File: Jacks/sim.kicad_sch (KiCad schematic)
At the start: 14 parts

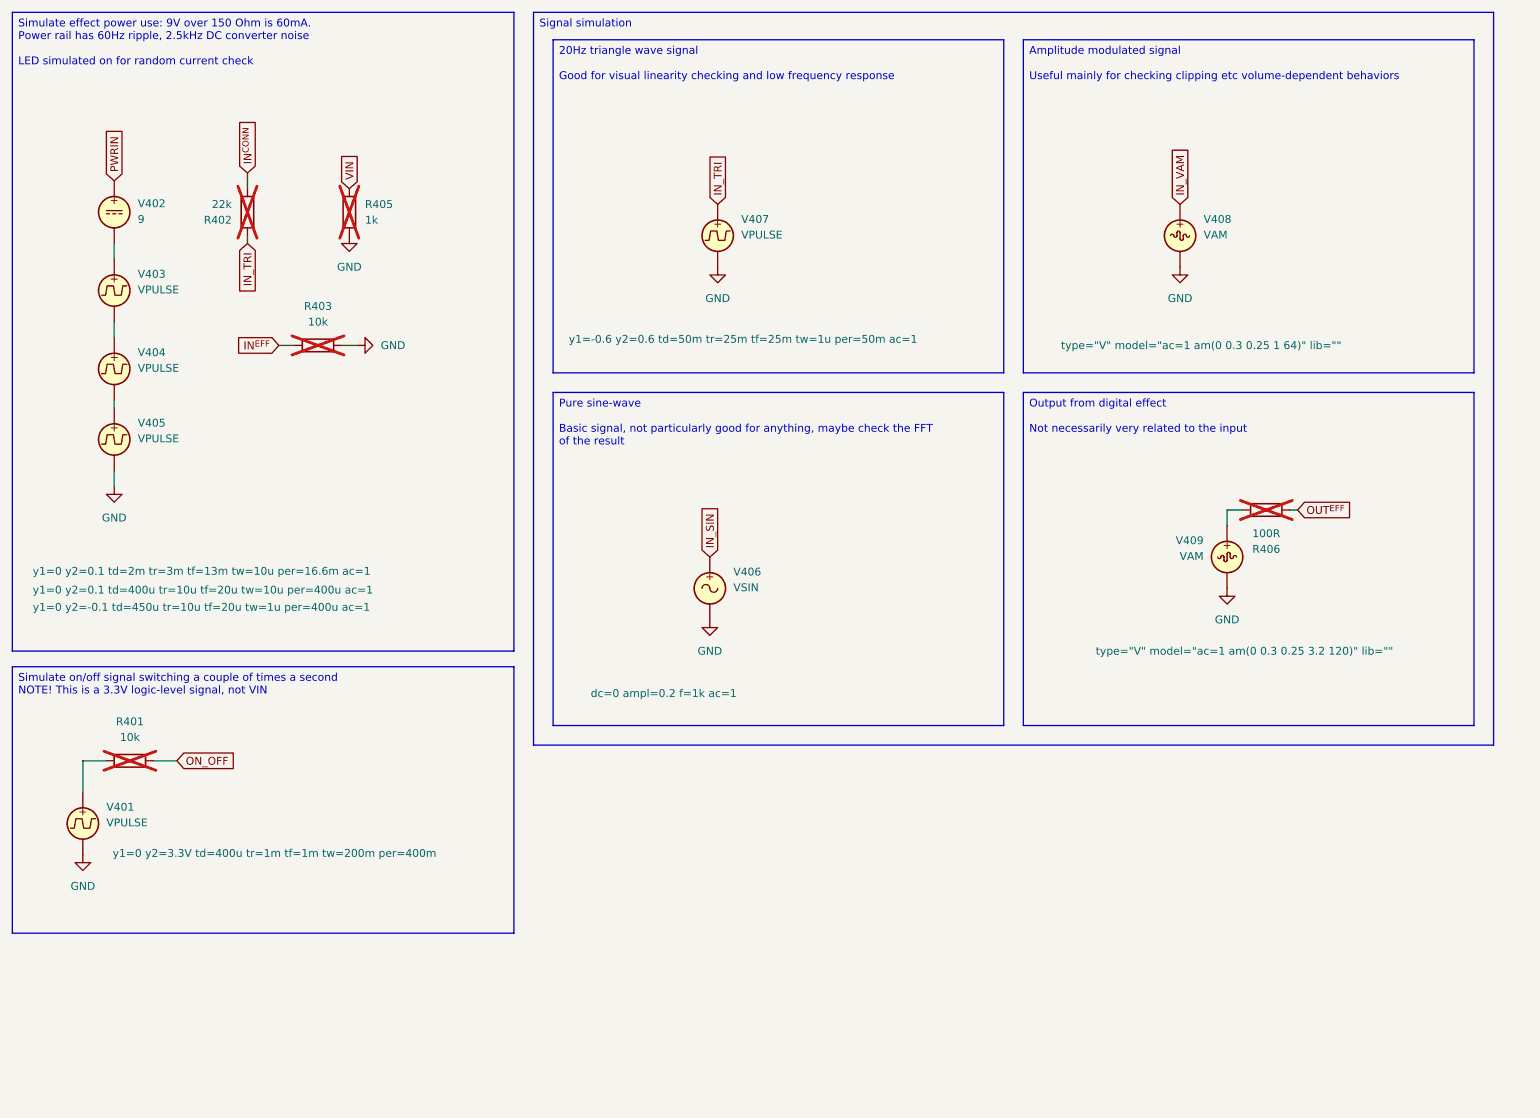
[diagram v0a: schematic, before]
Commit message: Trial attempt at different analog rail filtering
This does the +VA net a bit differently: by using a common collector
series follower transistor I can use much bigger resistors in the
lowpass filter because the current through the resistor is just the tiny
base current.

In fact, let's just make it the main filtering stage, and share the
resulting +VA rail for both the input stage and the output bias.  They
both need on the order of one mA of current, so assuming a DC current
gain (whether you call it h_{FE} or Beta) of roughly one hundred, we can
easily use a couple of 2k2 resistors and make it a 2nd order filter.

(The original used a single 220 Ohm resistor, so this increases that by
a factor of twenty, but then the h_{FE} will more than make up for it)

Of course, the small viltage drop over the resistors will now be almost
entirely dwarfed by the V_{BE} voltage drop of the transistor.  But if
it gives us a nice stable analog voltage rail, it should be worth the
small voltage drop.

I use a MOSFET for reverse polarity protection because I don't like the
voltage drop of a simple diode, but that's because the voltage drop
there would be just a negative.  Here there's a _reason_ for a voltage
drop.

Of course, I don't know how much it really helps with noise, but it
looks good in simulation, and I'm willing to at least do a test board
for this.

I'm just using the BC846 BJT I already have around.  It's a very average
cheap general-purpose transistor, I have no idea if this is any good.

Live and learn.  That's still the point of the whole project, after all.

While doing random trials, this also ends up DC-coupling the input side.
I probably shouldn't do two independent changes like this, but I'm too
lazy to do two separate boards.

Talking about separate boards: I wish KiCad had some good way to share
common circuits (some kind of "combination symbol" concept or something)
so that you could do explicitly different boards without having to
either do duplicate board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
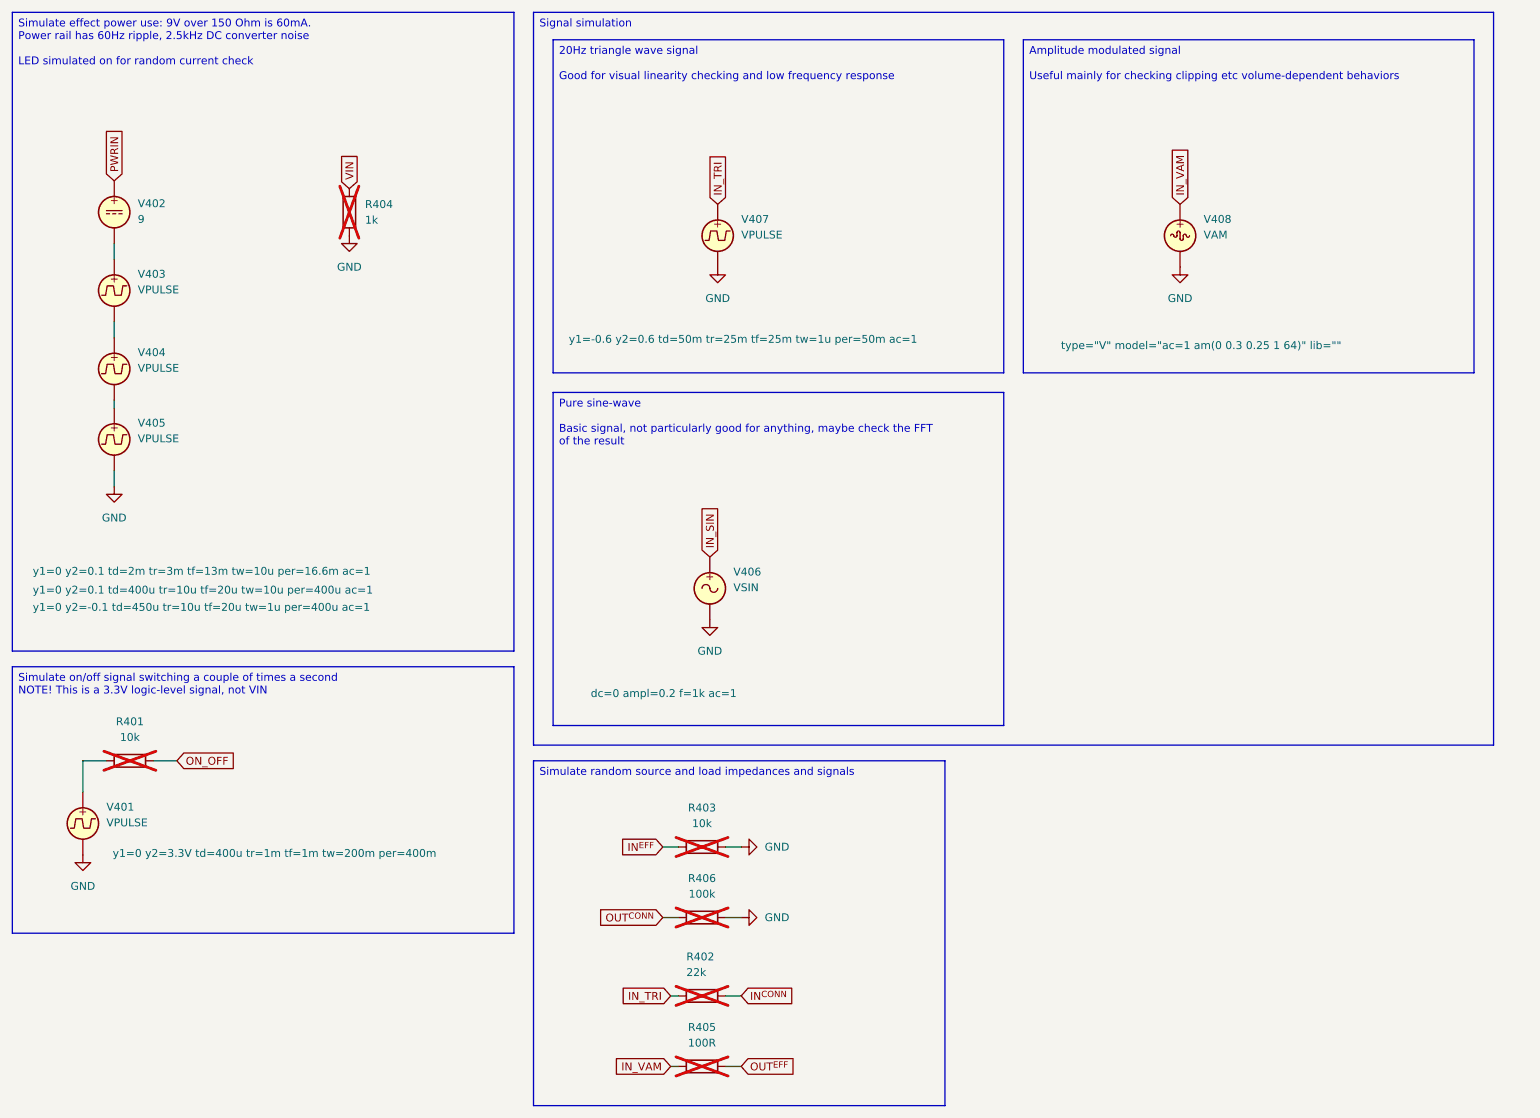
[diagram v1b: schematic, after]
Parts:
- removed V409: VAM, symbol Simulation_SPICE:VAM
- added R406: 100k, symbol Device:R
- renumbered R405 to R404, R406 to R405
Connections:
- net GND: now also R406.1
- net IN_VAM: now also R405.1
- new net OUT^{CONN}: R406.2
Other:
- moved on the sheet: R402, R403, R405
